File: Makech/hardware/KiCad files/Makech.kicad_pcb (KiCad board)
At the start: 2 copper layers, 54.9 x 88.5 mm, 50 parts, among them IC1 ULN2803, J1 SWD programmer, J2 USB_B_Micro, J3 ESP32-Exp, SW1 RST, SW2 SW_DPDT_x2, U1 ATSAMD21G18A-AU, U2 CONN_01X04, U3 AP2114_3.3v, X1 Screw_Terminal_1x02

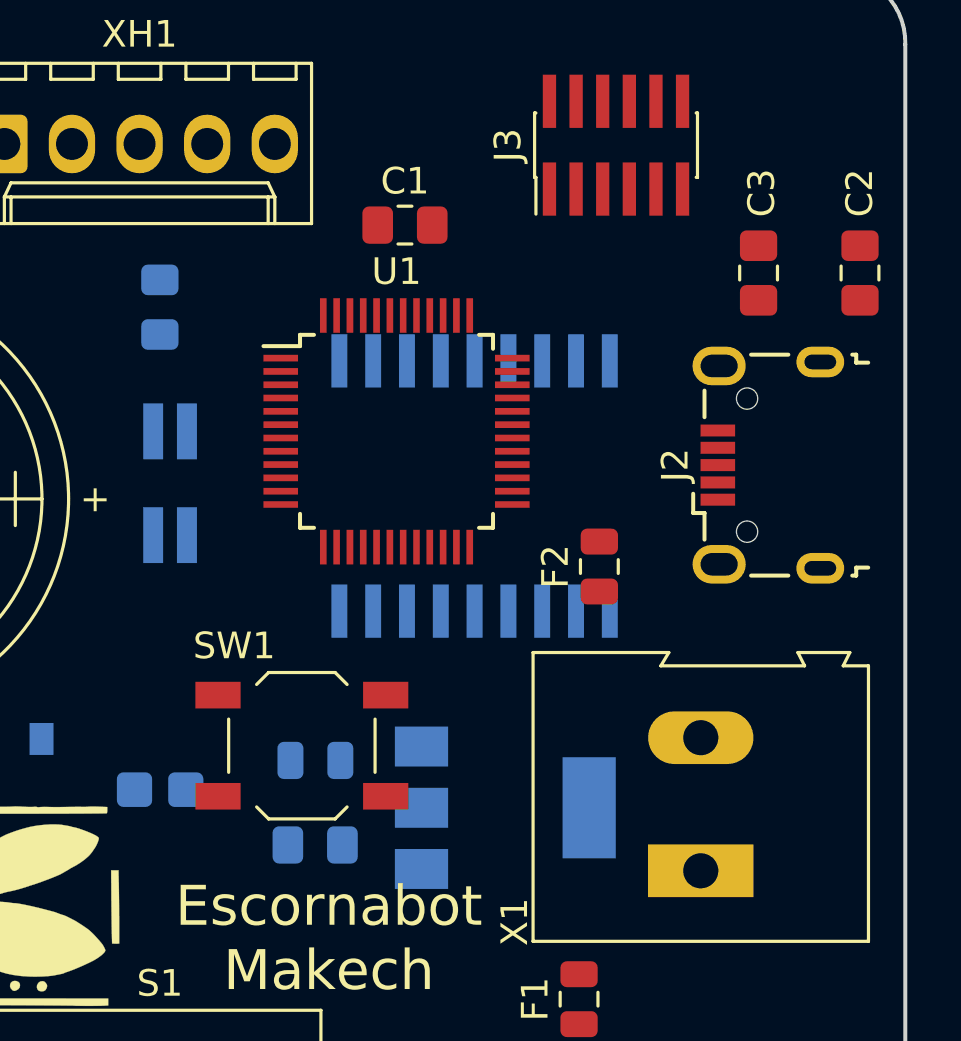
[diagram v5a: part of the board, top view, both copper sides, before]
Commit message: capacitors sources
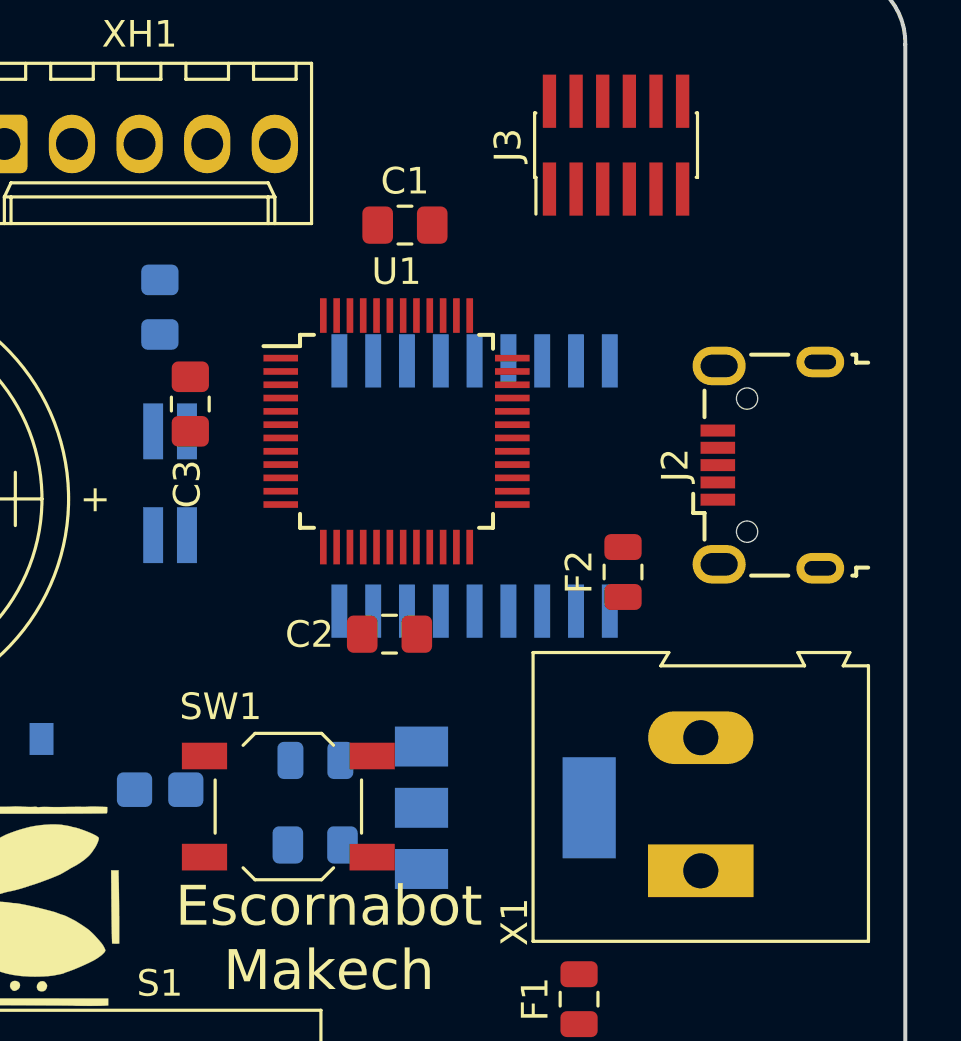
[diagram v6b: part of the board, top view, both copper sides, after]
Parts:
- moved C2 22.3 mm to (133.1, 81.3), turned to 0 degrees
- moved C3 21.9 mm to (125.6, 72.6), turned to 90 degrees
- moved SW1 2.34 mm to (129.3, 87.8)
- moved F2 0.91 mm to (141.9, 78.9)
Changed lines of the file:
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@@
-(kicad_pcb (version 20171130) (host pcbnew "(5.0.2)-1")
+(kicad_pcb (version 20171130) (host pcbnew "(5.0.1-3-g963ef8bb5)")
   (general
     (thickness 1.6)
@@
   )
   (module Button_Switch_SMD:SW_SPST_TL3342 (layer F.Cu)
-    (at 129.794 85.471)
+    (at 129.286 87.757)
     (descr "Low-profile SMD Tactile Switch, https://www.e-switch.com/system/asset/product_line/data_sheet/165/TL3342.pdf")
     (tags "SPST Tactile Switch")
@@
   )
   (module Capacitor_SMD:C_0805_2012Metric_Pad1.15x1.40mm_HandSolder (layer F.Cu)
-    (at 150.761765 67.713054 270)
+    (at 133.087 81.28)
     (descr "Capacitor SMD 0805 (2012 Metric), square (rectangular) end terminal, IPC_7351 nominal with elongated pad for handsoldering. (Body size source: https://docs.google.com/spreadsheets/d/1BsfQQcO9C6DZCsRaXUlFlo91Tg2WpOkGARC1WS5S8t0/edit?usp=sharing), generated with kicad-footprint-generator")
     (tags "capacitor handsolder")
     (attr smd)
-    (fp_text reference C2 (at -3.006554 0.012765 270) (layer F.SilkS)
-      (effects (font (size 1 1) (thickness 0.15)))
-    )
-    (fp_text value 0.1uF (at 0 1.65 270) (layer F.Fab)
+    (fp_text reference C2 (at -3.006554 0.012765) (layer F.SilkS)
+      (effects (font (size 1 1) (thickness 0.15)))
+    )
+    (fp_text value 0.1uF (at 0 1.65) (layer F.Fab)
       (effects (font (size 1 1) (thickness 0.15)))
     )
@@
     (fp_line (start 1.85 -0.95) (end 1.85 0.95) (layer F.CrtYd) (width 0.05))
     (fp_line (start 1.85 0.95) (end -1.85 0.95) (layer F.CrtYd) (width 0.05))
-    (fp_text user %R (at 0 0 270) (layer F.Fab)
+    (fp_text user %R (at 0 0) (layer F.Fab)
       (effects (font (size 0.5 0.5) (thickness 0.08)))
     )
-    (pad 1 smd roundrect (at -1.025 0 270) (size 1.15 1.4) (layers F.Cu F.Paste F.Mask) (roundrect_rratio 0.217391)
+    (pad 1 smd roundrect (at -1.025 0) (size 1.15 1.4) (layers F.Cu F.Paste F.Mask) (roundrect_rratio 0.217391)
       (net 7 +3V3))
-    (pad 2 smd roundrect (at 1.025 0 270) (size 1.15 1.4) (layers F.Cu F.Paste F.Mask) (roundrect_rratio 0.217391)
+    (pad 2 smd roundrect (at 1.025 0) (size 1.15 1.4) (layers F.Cu F.Paste F.Mask) (roundrect_rratio 0.217391)
       (net 1 GND))
     (model ${KISYS3DMOD}/Capacitor_SMD.3dshapes/C_0805_2012Metric.wrl
@@
   )
   (module Capacitor_SMD:C_0805_2012Metric_Pad1.15x1.40mm_HandSolder (layer F.Cu)
-    (at 146.951765 67.713054 270)
+    (at 125.603 72.635 90)
     (descr "Capacitor SMD 0805 (2012 Metric), square (rectangular) end terminal, IPC_7351 nominal with elongated pad for handsoldering. (Body size source: https://docs.google.com/spreadsheets/d/1BsfQQcO9C6DZCsRaXUlFlo91Tg2WpOkGARC1WS5S8t0/edit?usp=sharing), generated with kicad-footprint-generator")
     (tags "capacitor handsolder")
     (attr smd)
-    (fp_text reference C3 (at -3.006554 -0.114235 270) (layer F.SilkS)
-      (effects (font (size 1 1) (thickness 0.15)))
-    )
-    (fp_text value 0.1uF (at 0 1.65 270) (layer F.Fab)
+    (fp_text reference C3 (at -3.006554 -0.114235 90) (layer F.SilkS)
+      (effects (font (size 1 1) (thickness 0.15)))
+    )
+    (fp_text value 0.1uF (at 0 1.65 90) (layer F.Fab)
       (effects (font (size 1 1) (thickness 0.15)))
     )
@@
     (fp_line (start 1.85 -0.95) (end 1.85 0.95) (layer F.CrtYd) (width 0.05))
     (fp_line (start 1.85 0.95) (end -1.85 0.95) (layer F.CrtYd) (width 0.05))
-    (fp_text user %R (at 0 0 270) (layer F.Fab)
+    (fp_text user %R (at 0 0 90) (layer F.Fab)
       (effects (font (size 0.5 0.5) (thickness 0.08)))
     )
-    (pad 1 smd roundrect (at -1.025 0 270) (size 1.15 1.4) (layers F.Cu F.Paste F.Mask) (roundrect_rratio 0.217391)
+    (pad 1 smd roundrect (at -1.025 0 90) (size 1.15 1.4) (layers F.Cu F.Paste F.Mask) (roundrect_rratio 0.217391)
       (net 7 +3V3))
-    (pad 2 smd roundrect (at 1.025 0 270) (size 1.15 1.4) (layers F.Cu F.Paste F.Mask) (roundrect_rratio 0.217391)
+    (pad 2 smd roundrect (at 1.025 0 90) (size 1.15 1.4) (layers F.Cu F.Paste F.Mask) (roundrect_rratio 0.217391)
       (net 1 GND))
     (model ${KISYS3DMOD}/Capacitor_SMD.3dshapes/C_0805_2012Metric.wrl
@@
   )
   (module Fuse:Fuse_0805_2012Metric (layer F.Cu)
-    (at 140.97 78.74 90)
+    (at 141.859 78.9455 90)
     (descr "Fuse SMD 0805 (2012 Metric), square (rectangular) end terminal, IPC_7351 nominal, (Body size source: https://docs.google.com/spreadsheets/d/1BsfQQcO9C6DZCsRaXUlFlo91Tg2WpOkGARC1WS5S8t0/edit?usp=sharing), generated with kicad-footprint-generator")
     (tags resistor)

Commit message: PCB
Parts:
- moved F2 17.5 mm to (143.8, 61.6)
- moved J2 16.5 mm to (137.0, 62.0), turned to 180 degrees
- moved C3 16.0 mm to (141.5, 74.5)
- moved C1 11.5 mm to (125.0, 73.5), turned to 90 degrees
- moved D3 10.0 mm to (127.2, 85.0), turned to 180 degrees
- moved D2 9.18 mm to (127.2, 87.5), turned to 180 degrees
- moved J3 8.39 mm to (147.8, 68.5), turned to 0 degrees
- moved Z1 5.68 mm to (114.3, 78.7), turned to 135 degrees
- moved D1 4.36 mm to (127.8, 90.0), turned to 180 degrees
- moved C5 4.33 mm to (131.5, 90.2), turned to 270 degrees
- moved C6 3.92 mm to (122.5, 72.4)
- moved C4 3.65 mm to (131.5, 85.8), turned to 90 degrees
- moved J1 1.70 mm to (124.0, 77.1), turned to 90 degrees
- moved SW1 1.03 mm to (129.5, 86.8)
- moved U3 0.86 mm to (137.4, 86.9)
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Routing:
- net +6V: track 0.00 -> 54.7 mm, vias 0 -> 2
- net /MR4: track 0.00 -> 38.0 mm
- net /MR3: track 0.00 -> 36.4 mm
- net /MR2: track 0.00 -> 35.0 mm
- net /MR1: track 0.00 -> 33.6 mm
- net Net-(R5-Pad2): track 0.00 -> 28.3 mm
- net Net-(R2-Pad2): track 0.00 -> 28.1 mm
- net Net-(R3-Pad2): track 0.00 -> 23.1 mm
- net /ML4: track 0.00 -> 18.6 mm
- net Net-(F1-Pad1): track 0.00 -> 17.5 mm
- net /ML3: track 0.00 -> 15.7 mm
- net Net-(D1-Pad1): track 0.00 -> 14.3 mm, vias 0 -> 1
- net /ML2: track 0.00 -> 13.3 mm
- net Net-(R6-Pad2): track 0.00 -> 12.5 mm
- net Net-(R4-Pad2): track 0.00 -> 12.5 mm
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- added copper zone on B.Cu, net GND
- added copper zone on F.Cu, net GND
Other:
- net class Default: trace_width 0.25 -> 0.3
- net class source added: clearance 0.2, trace_width 0.5, via_dia 0.6, via_drill 0.4

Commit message: pistas
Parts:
- moved J2 1.57 mm to (137.2, 60.5)
- moved C3 1.32 mm to (141.7, 75.8)
- moved SW1 1.12 mm to (128.4, 87.2)
- moved C2 0.40 mm to (133.0, 82.2)
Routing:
- net /SCL: track 0.00 -> 62.3 mm, vias 0 -> 3
- net /A3: track 0.00 -> 45.0 mm, vias 0 -> 4
- net VCC: track 0.00 -> 44.0 mm, vias 0 -> 1
- net /D6: track 0.00 -> 43.2 mm, vias 0 -> 1
- net /D11: track 0.00 -> 43.2 mm, vias 0 -> 2
- net /D7: track 0.00 -> 35.4 mm, vias 0 -> 1
- net /ESP_RESET: track 0.00 -> 34.7 mm, vias 0 -> 2
- net /RX: track 0.00 -> 33.3 mm, vias 0 -> 2
- net /ESP_BUSY: track 0.00 -> 30.5 mm, vias 0 -> 2
- net Net-(D1-Pad1): track 14.3 -> 43.1 mm
- net /ESP_SCK: track 0.00 -> 28.1 mm, vias 0 -> 2
- net /TX: track 0.00 -> 26.5 mm, vias 0 -> 2
- net /ESP_GPIO: track 0.00 -> 25.6 mm
- net +3V3: track 9.97 -> 31.9 mm, vias 0 -> 1
- net +6V: track 54.7 -> 76.4 mm
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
